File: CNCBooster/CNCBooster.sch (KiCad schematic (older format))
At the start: 22 parts, among them J1 TI_BOOSTER_40_J1, J2 TI_BOOSTER_40_J2, J3 TI_BOOSTER_40_J3, J4 TI_BOOSTER_40_J4, J5 CONN_3, M1 Pololu_A4988, M2 Pololu_A4988, M3 Pololu_A4988, M4 Pololu_A4988, M5 Pololu_A4988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

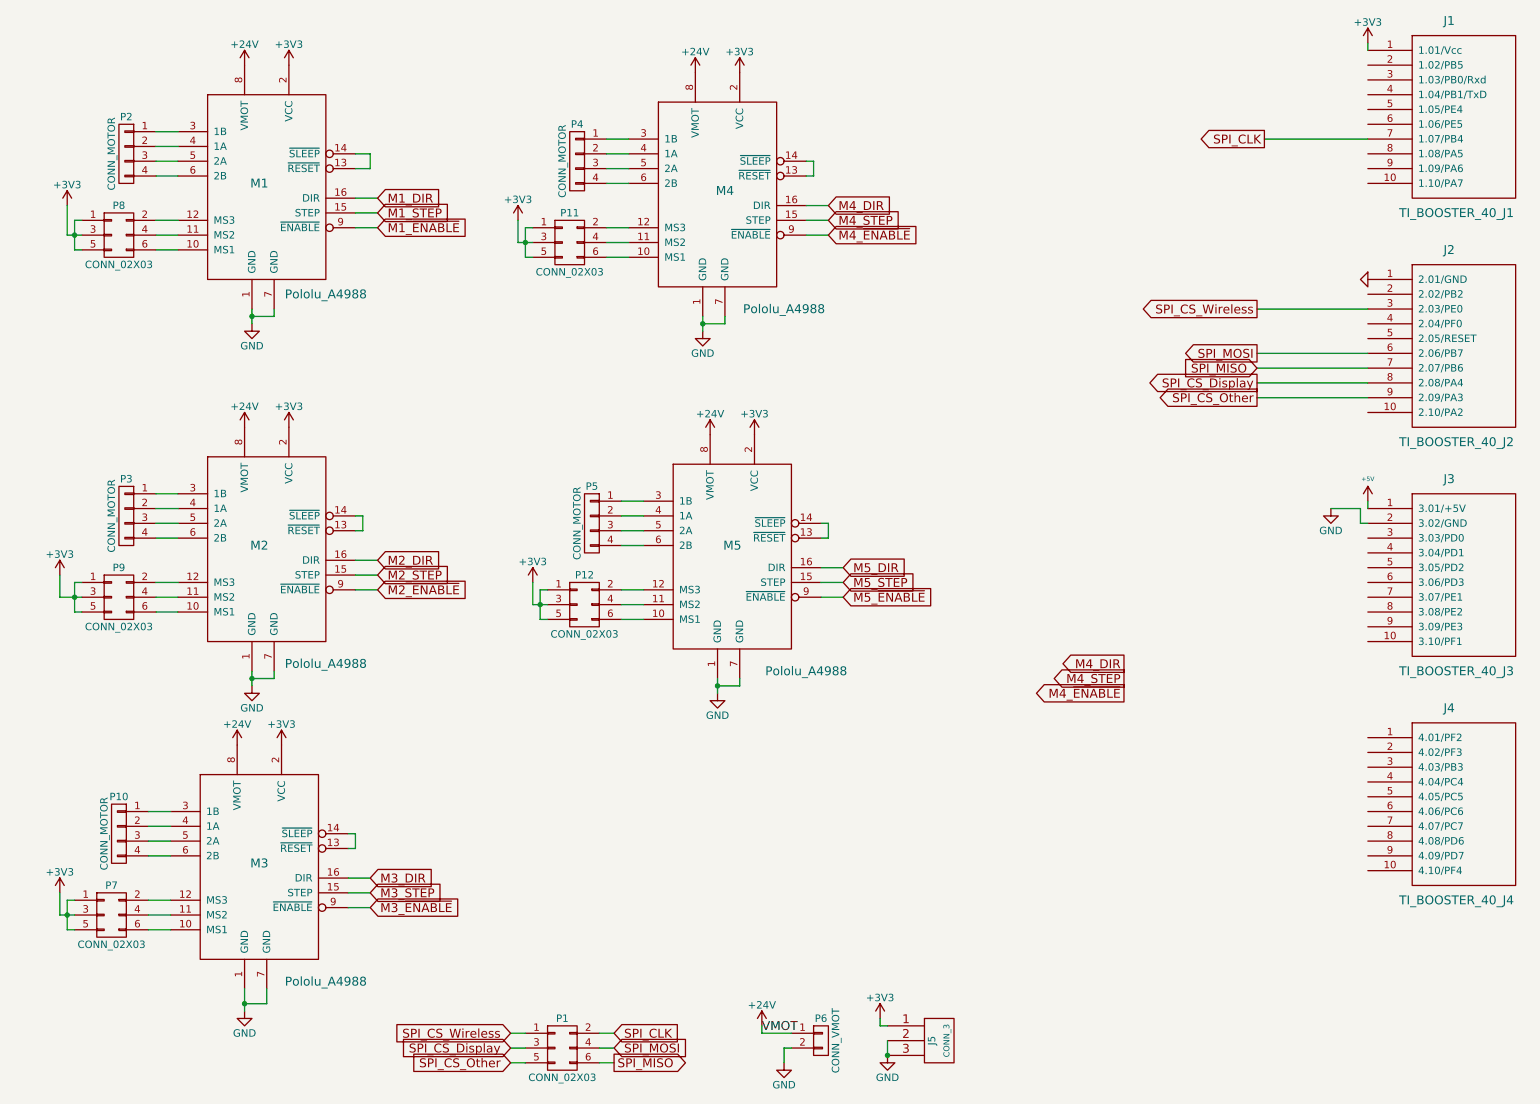
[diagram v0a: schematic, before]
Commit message: Motor Wiring Complete
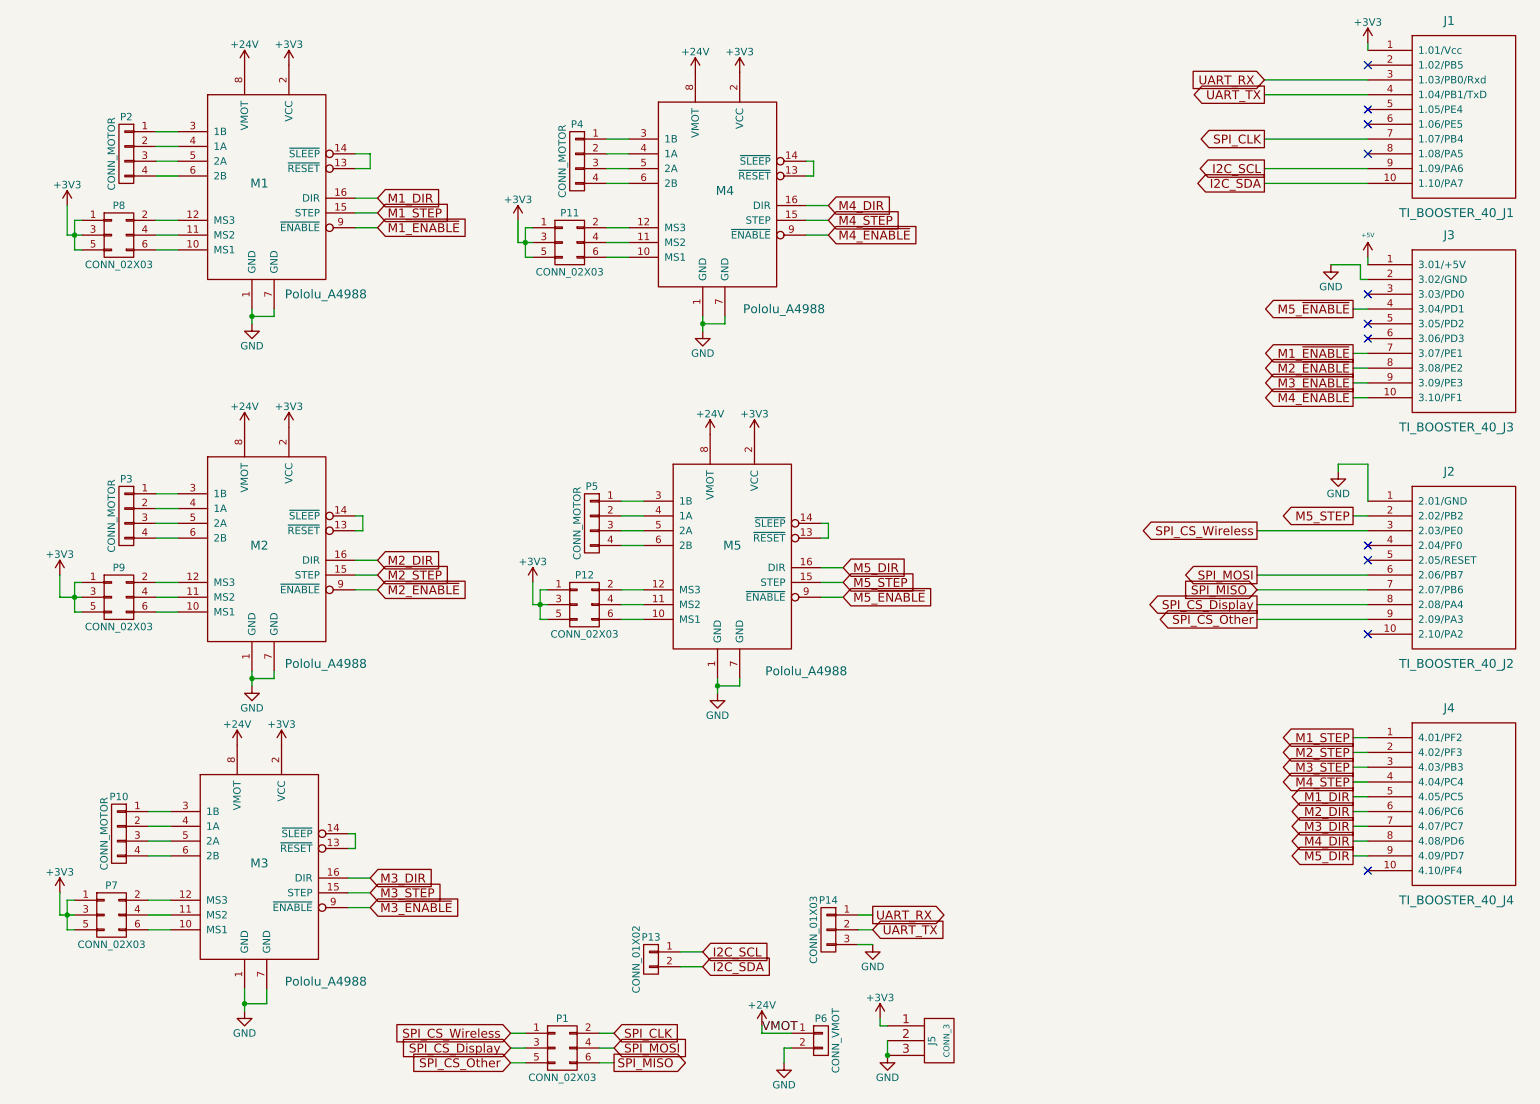
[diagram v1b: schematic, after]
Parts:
- added P13: CONN_01X02, symbol CONN_01X02
- added P14: CONN_01X03, symbol CONN_01X03
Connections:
- net GND: now also P14.3 (P3)
- net M1_DIR: now also J4.5 (4.05/PC5)
- net M1_STEP: now also J4.1 (4.01/PF2)
- net M1_~ENABLE: now also J3.7 (3.07/PE1)
- net M2_DIR: now also J4.6 (4.06/PC6)
- net M2_STEP: now also J4.2 (4.02/PF3)
- net M2_~ENABLE: now also J3.8 (3.08/PE2)
- net M3_DIR: now also J4.7 (4.07/PC7)
- net M3_STEP: now also J4.3 (4.03/PB3)
- net M3_~ENABLE: now also J3.9 (3.09/PE3)
- net M4_DIR: now also J4.8 (4.08/PD6)
- net M4_STEP: now also J4.4 (4.04/PC4)
- net M4_~ENABLE: now also J3.10 (3.10/PF1)
- net M5_DIR: now also J4.9 (4.09/PD7)
- net M5_STEP: now also J2.2 (2.02/PB2)
- net M5_~ENABLE: now also J3.4 (3.04/PD1)
- net I2C_SDA: now reaches J1.10 (1.10/PA7)
- net I2C_SDA: now also P13.2 (P2)
- net UART_RX: now reaches J1.3 (1.03/PB0/Rxd)
- net UART_RX: now also P14.1 (P1)
- net UART_TX: now reaches J1.4 (1.04/PB1/TxD)
- net UART_TX: now also P14.2 (P2)
- net I2C_SCL: now reaches J1.9 (1.09/PA6)
- net I2C_SCL: now also P13.1 (P1)
- no-connect marks 0 -> 11
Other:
- moved on the sheet: J2, J3

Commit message: Removed reduntant UART, added limit switches for 4 motors
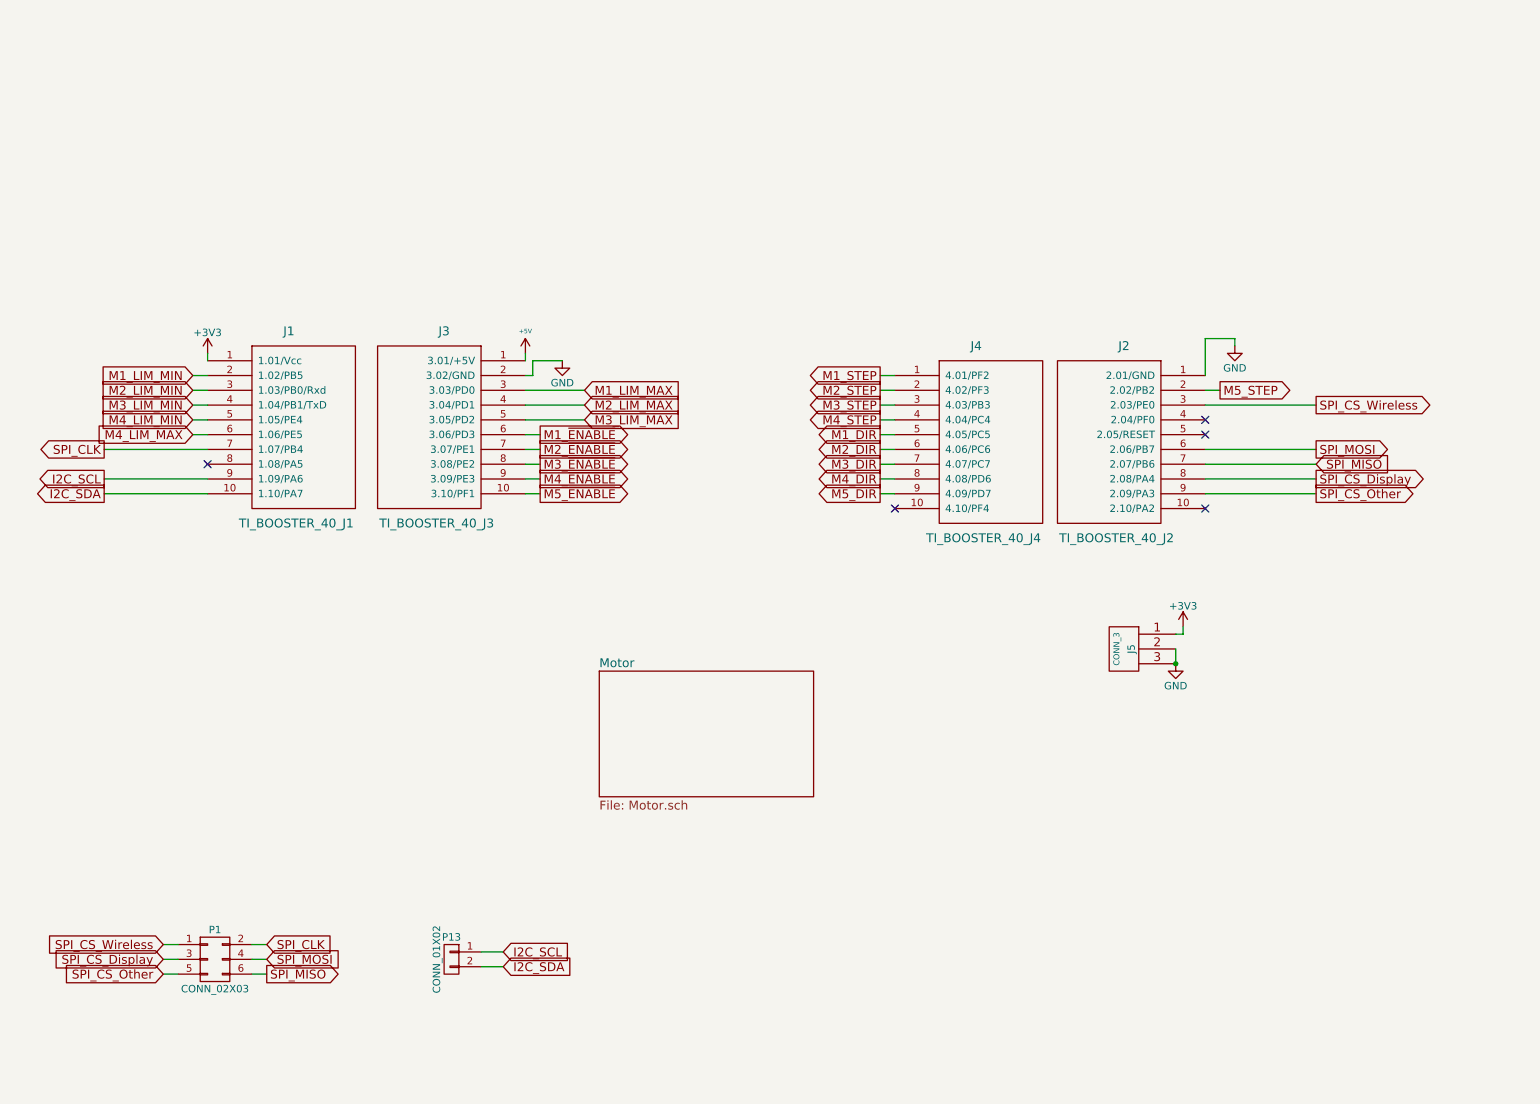
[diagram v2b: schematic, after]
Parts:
- removed M1, M2, M3, M4, M5: Pololu_A4988, symbol Pololu_A4988
- removed P10, P2, P3, P4, P5: CONN_MOTOR, symbol CONN_MOTOR
- removed P11, P12, P7, P8, P9: CONN_02X03, symbol CONN_02X03
- removed P14: CONN_01X03, symbol CONN_01X03
- removed P6: CONN_VMOT, symbol CONN_VMOT
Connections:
- net M1_~ENABLE: now also J3.6 (3.06/PD3); no longer J3.7 (3.07/PE1)
- net M2_~ENABLE: now also J3.7 (3.07/PE1); no longer J3.8 (3.08/PE2)
- net M3_~ENABLE: now also J3.8 (3.08/PE2); no longer J3.9 (3.09/PE3)
- net M4_~ENABLE: now also J3.9 (3.09/PE3); no longer J3.10 (3.10/PF1)
- net M5_~ENABLE: now also J3.10 (3.10/PF1); no longer J3.4 (3.04/PD1)
- net M1_LIM_MIN: now reaches J1.2 (1.02/PB5)
- net M4_LIM_MIN: now reaches J1.5 (1.05/PE4)
- net M4_LIM_MAX: now reaches J1.6 (1.06/PE5)
- net M1_LIM_MAX: now reaches J3.3 (3.03/PD0)
- net M3_LIM_MAX: now reaches J3.5 (3.05/PD2)
- net UART_RX renamed M2_LIM_MIN
- net UART_TX renamed M3_LIM_MIN
- new net M2_LIM_MAX: J3.4 (3.04/PD1)
- no-connect marks 11 -> 5
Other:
- moved on the sheet: J1, J2, J3, J4, J5, P1, P13
